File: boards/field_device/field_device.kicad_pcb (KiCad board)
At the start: 4 copper layers, 68 parts, among them J1 Conn_01x05_Pin, J2 Conn_01x02_Pin, SW1 SW_SPST, U1 CHT20MEMS, U2 STM32C011F6Px, U3 SPA06-003, U4 CN3163, U5 HX8001-AJC, U6 SX1262IMLTRT, U7 TPS63900, Y1 Crystal_GND24

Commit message: route regulator
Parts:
- removed the L1 at (164.7, 108.1)
- removed the L1 at (179.7, 60.7)
- added L1: 2u2, UnEasy-LCSC:IND-SMD_L4.0-W4.0_B, F.Cu at (179.8, 60.4)
- R15: footprint Resistor_SMD:R_0402_1005Metric_Pad0.72x0.64mm_HandSolder -> Resistor_SMD:R_0603_1608Metric
- moved R15 71.8 mm to (137.1, 102.0), turned to 90 degrees
- moved D2 71.1 mm to (138.0, 99.7), turned to 180 degrees
- moved D3 70.2 mm to (138.0, 97.7), turned to 180 degrees
- moved BT1 63.0 mm to (141.6, 91.7)
- moved R14 60.9 mm to (147.8, 98.6), turned to 90 degrees
- moved U4 59.6 mm to (143.5, 98.6), turned to 90 degrees
- moved SC1 59.2 mm to (145.4, 91.8), turned to 180 degrees
- moved C8 58.8 mm to (141.5, 95.2)
- moved C7 54.8 mm to (145.6, 95.2), turned to 180 degrees
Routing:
- net /power_source/solar_pwr: track 0.00 -> 24.7 mm
- net GND: track 9.00 -> 25.3 mm, vias 0 -> 7
- net /power_source/regulator/Vin: track 1.53 -> 11.3 mm
- net Net-(D2-A): track 0.00 -> 3.45 mm
- net /power_source/chrg: track 0.00 -> 1.95 mm
- net /power_source/done: track 0.00 -> 1.91 mm
- net Net-(U4-ISET): track 0.00 -> 1.42 mm

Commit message: route more stuff
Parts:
- removed the C10 at (183.2, 107.5)
- removed C11: 22u, Capacitor_SMD:C_0805_2012Metric_Pad1.18x1.45mm_HandSolder
- removed C12: 1n5, Capacitor_SMD:C_0402_1005Metric_Pad0.74x0.62mm_HandSolder
- removed the C9 at (183.7, 105.3)
- removed D4: PWR, LED_SMD:LED_0603_1608Metric_Pad1.05x0.95mm_HandSolder
- removed the R16 at (174.3, 98.2)
- removed R17: 10k, Resistor_SMD:R_0402_1005Metric_Pad0.72x0.64mm_HandSolder
- removed R18: 340k, Resistor_SMD:R_0402_1005Metric_Pad0.72x0.64mm_HandSolder
- removed R19: 200k, Resistor_SMD:R_0402_1005Metric_Pad0.72x0.64mm_HandSolder
- removed R20: 15k, Resistor_SMD:R_0402_1005Metric_Pad0.72x0.64mm_HandSolder
- removed R21: 60k4, Resistor_SMD:R_0402_1005Metric_Pad0.72x0.64mm_HandSolder
- removed U5: HX8001-AJC, LCSC downloads:MSOP-10_L3.0-W3.0-P0.50-LS5.0-BL
- C1: footprint Capacitor_SMD:C_0603_1608Metric_Pad1.08x0.95mm_HandSolder -> Capacitor_SMD:C_0603_1608Metric
- C5, C6: footprint Capacitor_SMD:C_0402_1005Metric_Pad0.74x0.62mm_HandSolder -> Capacitor_SMD:C_0603_1608Metric
- R13: footprint Resistor_SMD:R_0402_1005Metric_Pad0.72x0.64mm_HandSolder -> Resistor_SMD:R_0603_1608Metric
- R15: footprint Resistor_SMD:R_0603_1608Metric -> Capacitor_SMD:C_0603_1608Metric_Pad1.08x0.95mm_HandSolder
- moved D1 69.4 mm to (220.9, 76.6), turned to 0 degrees
- moved R11 66.9 mm to (217.0, 82.0), turned to 0 degrees
- moved C2 64.7 mm to (204.6, 78.6)
- moved C4 64.7 mm to (204.6, 76.3)
- moved J1 64.7 mm to (212.2, 70.3)
- moved R4 64.7 mm to (203.5, 78.7)
- moved R5 64.7 mm to (214.4, 80.3)
- moved R6 64.7 mm to (214.4, 79.1)
- moved R8 64.7 mm to (214.4, 78.0)
- moved C3 64.7 mm to (201.7, 76.7)
- moved U2 64.7 mm to (209.3, 77.1)
- moved R7 55.6 mm to (217.0, 76.0)
- moved R3 55.5 mm to (217.0, 74.0)
- moved R10 52.6 mm to (217.0, 80.0)
- moved R12 52.6 mm to (217.0, 84.0)
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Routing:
- net +3.3V: track 1.73 -> 13.2 mm, vias 0 -> 3
- net GND: track 25.3 -> 32.6 mm, vias 7 -> 9
- net /power_source/solar_pwr: track 24.7 -> 21.6 mm
- net Net-(U3-CSB): track 0.00 -> 1.96 mm
- net Net-(U1-VDD): track 0.00 -> 1.75 mm

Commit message: routed everything
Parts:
- R3: footprint Resistor_SMD:R_0402_1005Metric_Pad0.72x0.64mm_HandSolder -> Resistor_SMD:R_0603_1608Metric_Pad0.98x0.95mm_HandSolder
- moved AE1 200.0 mm to (1.66, 1.77)
- moved D3 67.7 mm to (205.2, 106.4), turned to -90 degrees
- moved D2 67.2 mm to (205.2, 102.8), turned to 90 degrees
- moved R15 67.2 mm to (205.2, 99.4), turned to -90 degrees
- moved BT1 64.0 mm to (202.5, 111.4), turned to 180 degrees
- moved C8 62.5 mm to (202.6, 107.9), turned to 180 degrees
- moved U4 57.3 mm to (200.6, 104.5), turned to -90 degrees
- moved SC1 56.7 mm to (198.7, 111.3), turned to 0 degrees
- moved C7 54.4 mm to (198.5, 107.9), turned to 0 degrees
- moved R14 48.8 mm to (196.2, 104.5), turned to -90 degrees
- moved C16 42.2 mm to (211.8, 95.4), turned to 90 degrees
- moved C18 41.1 mm to (210.8, 97.0)
- moved C19 41.1 mm to (210.8, 98.0)
- moved C22 40.9 mm to (210.6, 103.8)
- moved C21 40.8 mm to (210.6, 101.5)
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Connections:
- J1 pad 1: GND -> /MCU/SWDIO
- J1 pad 2: +3.3V -> /MCU/SWDCLK
- J1 pad 3: /MCU/SWDCLK -> GND
- J1 pad 4: /MCU/SWDIO -> +3.3V
- R5 pad 1: /MCU/RF_NSS -> /MCU/MCU_NSS
- R6 pad 1: /MCU/RF_SCK -> /MCU/MCU_SCK
- R7 pad 1: /MCU/RF_MISO -> /MCU/MCU_MISO
- R8 pad 1: /MCU/RF_MOSI -> /MCU/MCU_MOSI
- U2 pad 11: /MCU/RF_NSS -> /MCU/MCU_NSS
- U2 pad 12: /MCU/RF_SCK -> /MCU/MCU_SCK
- U2 pad 13: /MCU/RF_MISO -> /MCU/MCU_MISO
- U2 pad 14: /MCU/RF_MOSI -> /MCU/MCU_MOSI
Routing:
- net GND: track 32.6 -> 67.1 mm, vias 9 -> 24
- net /MCU/NRST: track 0.00 -> 34.4 mm, vias 0 -> 2
- net /MCU/MCU_MISO: track 0.00 -> 30.8 mm, vias 0 -> 2
- net /MCU/SCL_bus: track 0.00 -> 26.8 mm, vias 0 -> 3
- net /MCU/SDA_bus: track 0.00 -> 26.1 mm, vias 0 -> 3
- net +3.3V: track 13.2 -> 38.7 mm, vias 3 -> 10
- net /MCU/RF_MOSI: track 0.00 -> 25.4 mm, vias 0 -> 2
- net /MCU/RF_SCK: track 0.00 -> 19.6 mm, vias 0 -> 2
- net /MCU/RF_NRST: track 0.00 -> 17.0 mm
- net /MCU/RF_NSS: track 0.00 -> 16.6 mm, vias 0 -> 2
- net /MCU/RF_DIO1: track 0.00 -> 15.4 mm
- net /power_source/regulator/Vin: track 11.3 -> 26.2 mm
- net /MCU/RF_BUSY: track 0.00 -> 14.2 mm
- net Net-(D2-A): track 3.72 -> 13.9 mm, vias 0 -> 2
- net /MCU/LOG_MCU_RX: track 0.00 -> 8.96 mm
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- added copper zone on F.Cu, net +3.3V
- added copper zone on F.Cu, net /power_source/regulator/Vin
- added copper zone on F.Cu, net GND
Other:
- board outline added: 24.2 x 44.2 mm

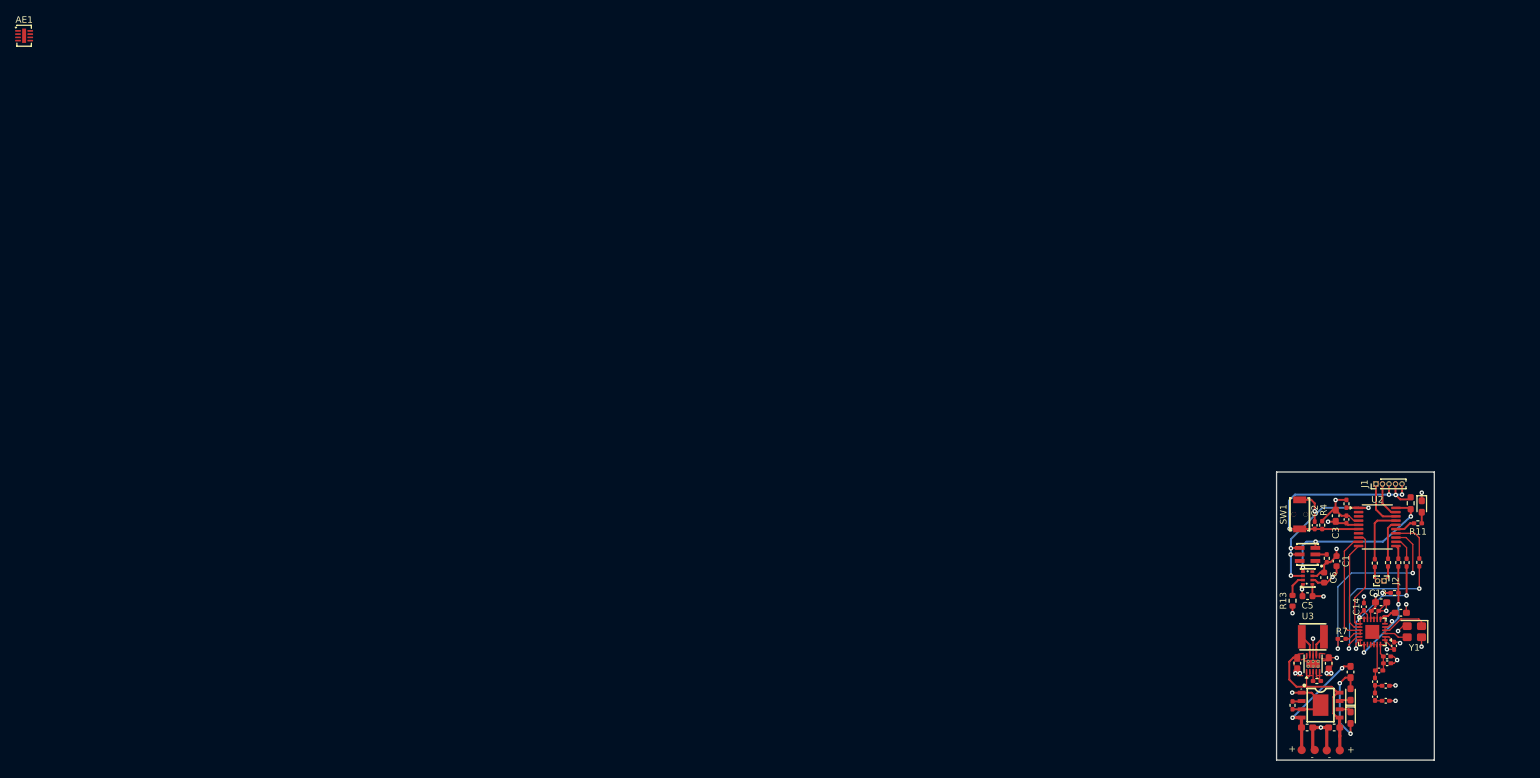
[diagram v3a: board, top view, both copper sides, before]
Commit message: moved modules to make space for antenna
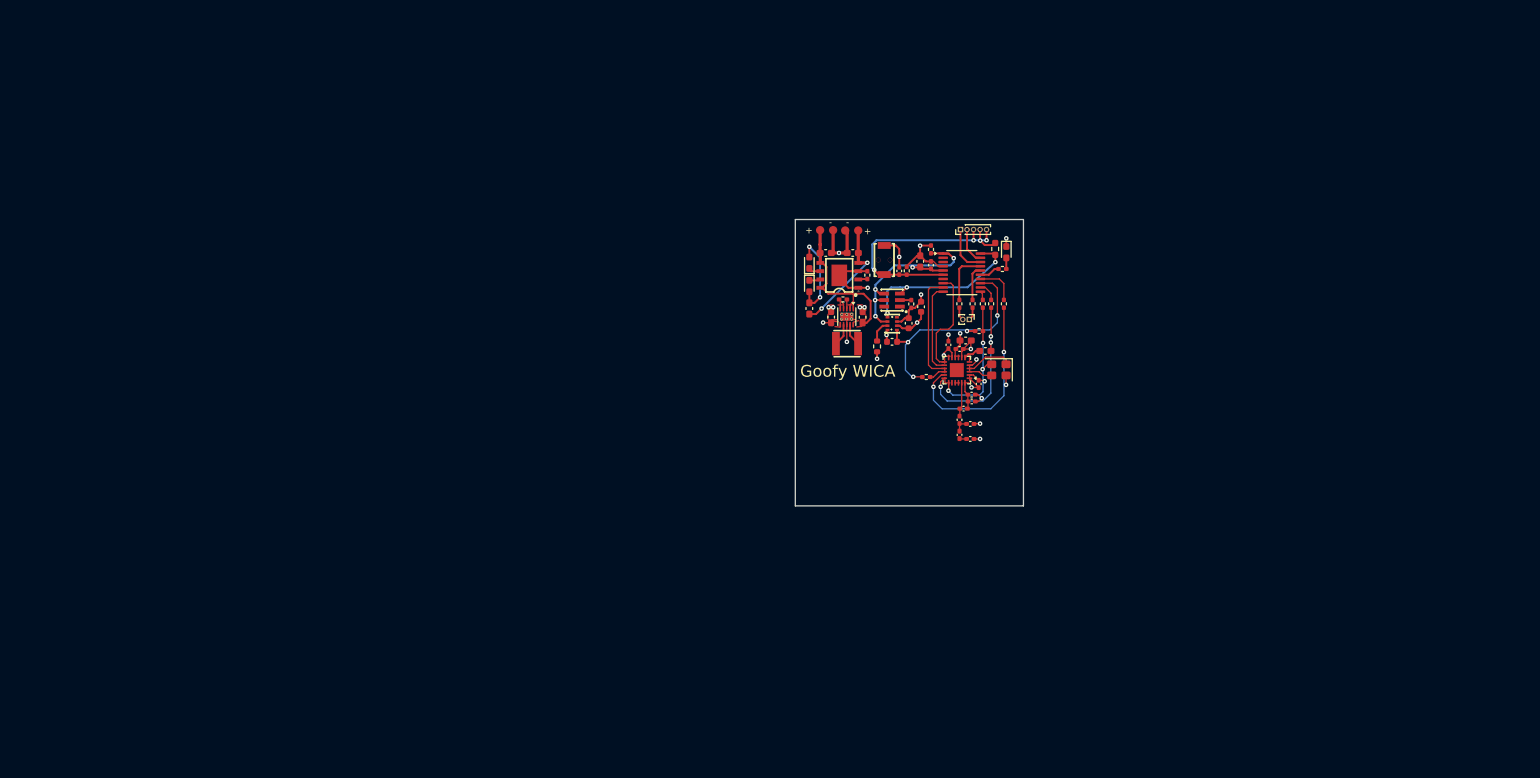
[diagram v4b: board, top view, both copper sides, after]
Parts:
- removed AE1: Antenna, Package_DFN_QFN:DFN-8-1EP_2x3mm_P0.5mm_EP0.61x2.2mm
- moved BT1 111.4 mm to (124.8, 31.6), turned to 0 degrees
- moved D3 108.5 mm to (122.1, 36.6), turned to 90 degrees
- moved C8 106.7 mm to (124.6, 35.1), turned to 0 degrees
- moved SC1 106.1 mm to (128.6, 31.6), turned to 180 degrees
- moved D2 104.0 mm to (122.1, 40.2), turned to -90 degrees
- moved C7 100.8 mm to (128.8, 35.1), turned to 180 degrees
- moved R15 100.0 mm to (122.1, 43.6), turned to 90 degrees
- moved U4 99.0 mm to (126.7, 38.5), turned to 90 degrees
- moved R16 93.3 mm to (127.3, 42.2), turned to 180 degrees
- moved C10 93.0 mm to (125.5, 44.9), turned to 90 degrees
- moved R14 92.8 mm to (131.0, 38.5), turned to 90 degrees
- moved U7 89.2 mm to (127.9, 44.9), turned to -90 degrees
- moved C9 85.2 mm to (130.3, 45.0), turned to 90 degrees
- moved L1 84.4 mm to (127.9, 49.0), turned to 0 degrees
- moved C13 75.3 mm to (146.1, 48.5)
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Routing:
- net /MCU/RF_MOSI: track 25.4 -> 30.6 mm
- net /MCU/RF_SCK: track 19.6 -> 24.5 mm
- net /MCU/RF_NSS: track 16.6 -> 19.9 mm
- net /MCU/RF_DIO1: track 15.4 -> 16.2 mm
- net /MCU/LOG_MCU_RX: track 8.96 -> 8.20 mm
- net /MCU/LOG_MCU_TX: track 6.15 -> 5.47 mm
- net /MCU/MCU_NSS: track 2.09 -> 1.41 mm
- net /MCU/MCU_SCK: track 3.70 -> 3.02 mm
- net /MCU/MCU_MOSI: track 7.05 -> 6.40 mm
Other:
- board size 24.2 x 44.2 mm -> 35 x 43.9 mm
- board text added: "Goofy WICA"
